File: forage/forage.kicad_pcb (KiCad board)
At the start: 2 copper layers, 308 x 79.4 mm, 68 parts, among them J1 Conn_01x04_MountingPin, Q1 AO3400A, U1 STM32G431RBTx, U2 XC6206P322MR

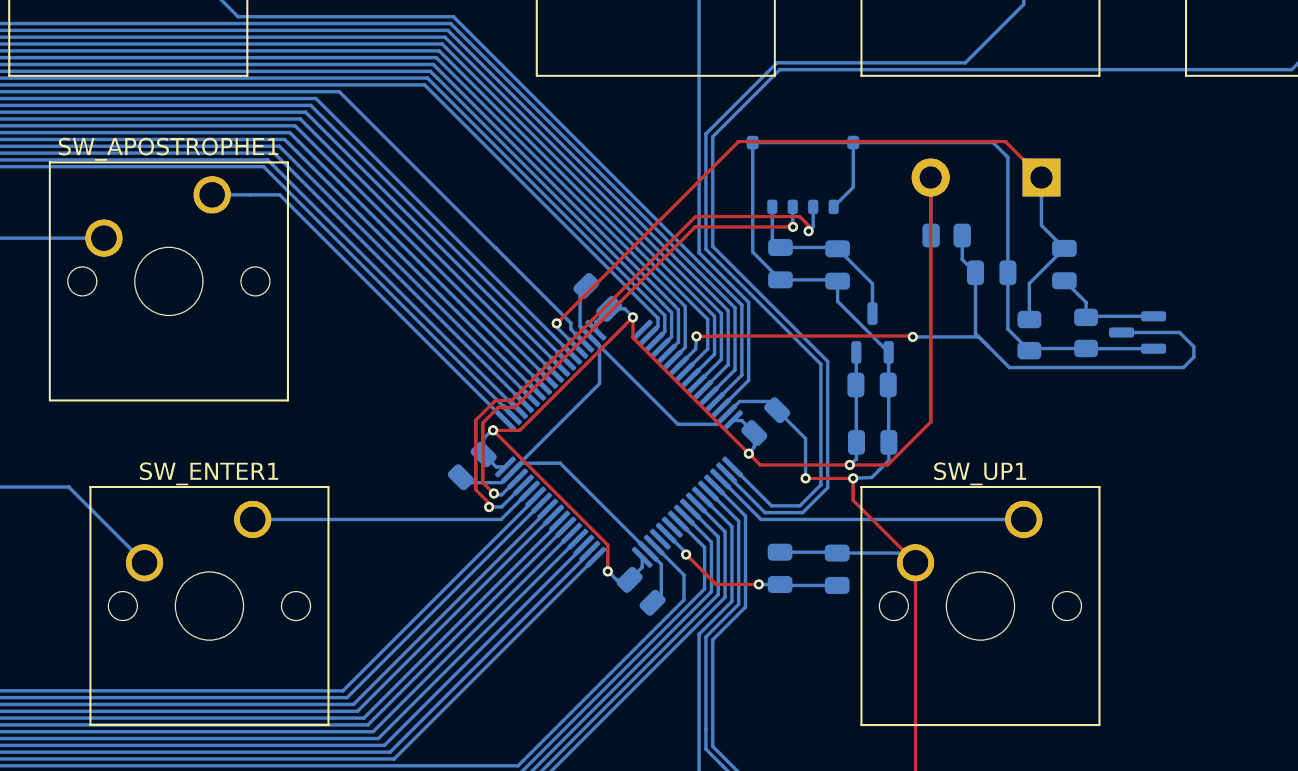
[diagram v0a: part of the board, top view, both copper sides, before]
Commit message: move connector so D+/D- has a direct path
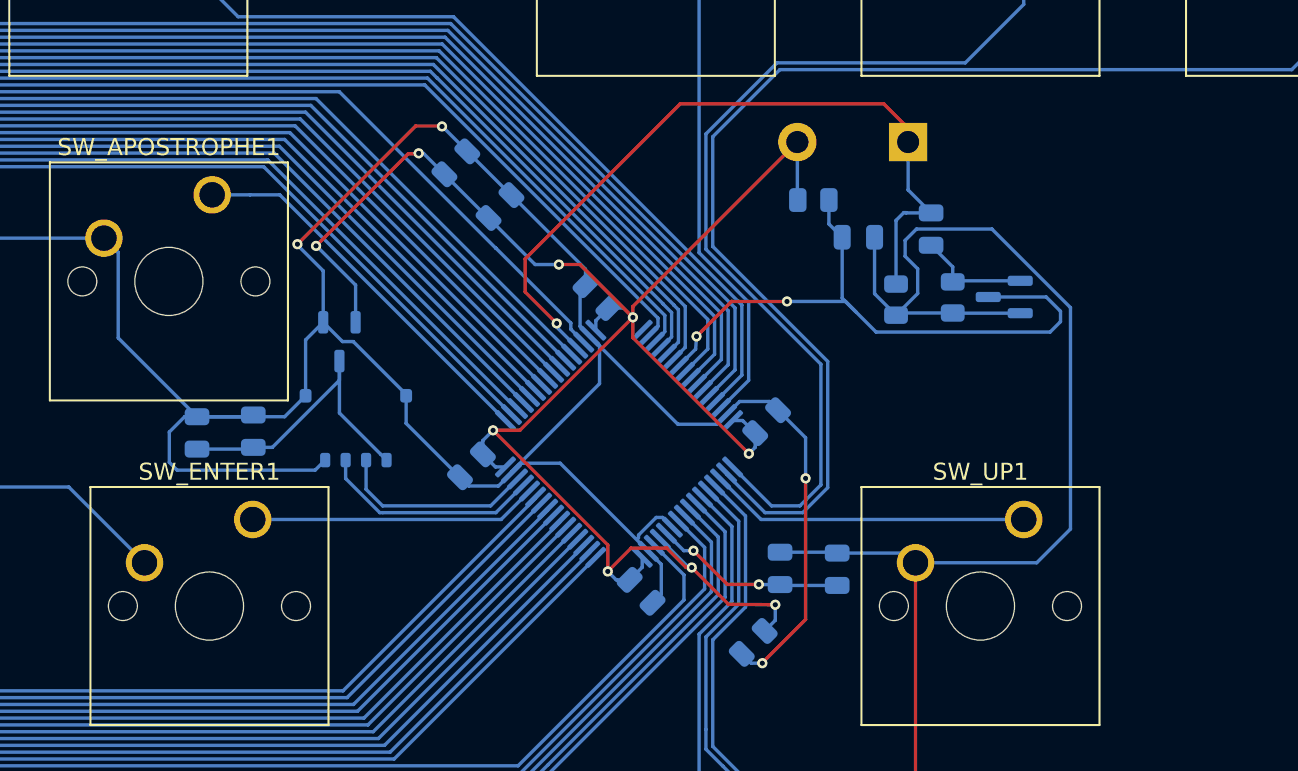
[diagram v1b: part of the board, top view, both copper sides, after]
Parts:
- added C13: 100nF, Capacitor_SMD:C_0805_2012Metric, B.Cu at (316.9, 154.5)
- C12: value 100nF -> 4.7uF
- C6: value 4.7uF -> 100nF
- moved C7 35.7 mm to (284.2, 142.2), turned to 90 degrees
- moved C8 35.7 mm to (287.5, 142.1), turned to 90 degrees
- moved U2 31.3 mm to (292.6, 136.9), turned to -90 degrees
- moved J1 30.2 mm to (293.5, 142.0)
- moved C9 27.7 mm to (299.4, 126.4), turned to 45 degrees
- moved C12 24.1 mm to (302.0, 129.0), turned to 45 degrees
- moved C3 12.4 mm to (310.3, 151.5), turned to -45 degrees
- moved C11 8.10 mm to (323.0, 130.8)
- moved Q1 8.10 mm to (331.6, 134.3)
- moved R1 8.10 mm to (325.2, 134.4)
- moved R2 8.10 mm to (328.6, 134.3)
- moved SW_RESET1 8.10 mm to (326.0, 125.2)
- moved C10 8.10 mm to (327.3, 130.3)
- moved R3 8.10 mm to (320.4, 128.6)
- moved C6 6.34 mm to (317.7, 141.6), turned to 45 degrees
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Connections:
- J1 pad 1: +5V -> GND
- J1 pad 2: D+ -> D-
- J1 pad 3: D- -> D+
- J1 pad 4: GND -> +5V
- U1 pad 27: unconnected-(U1-VSSA-Pad27) -> GND
- U1 pad 29: unconnected-(U1-VDDA-Pad29) -> +3.3V
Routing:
- net GND: track 1305.6 -> 1384.2 mm, vias 2 -> 4
- net +3.3V: track 82.4 -> 110.4 mm, vias 5 -> 9
- net D-: track 34.8 -> 13.0 mm, vias 2 -> 0
- net D+: track 30.8 -> 11.7 mm, vias 2 -> 0
- net +5V: track 10.6 -> 18.1 mm
- net RESET: track 45.0 -> 38.0 mm
- net BOOT: track 45.6 -> 45.1 mm

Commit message: move caps around a little bit to reduce vias
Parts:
- moved C9 14.6 mm to (293.3, 139.6), turned to 180 degrees
- moved C12 11.2 mm to (293.4, 136.1), turned to 180 degrees
- moved J1 6.28 mm to (294.8, 148.1)
- moved U2 5.96 mm to (293.3, 142.8)
- moved C10 3.01 mm to (324.5, 131.5)
- moved C11 3.01 mm to (320.3, 131.9)
- moved Q1 3.01 mm to (328.8, 135.5)
- moved R2 3.01 mm to (325.8, 135.5)
- moved R3 3.01 mm to (317.6, 129.8)
- moved SW_RESET1 3.01 mm to (323.2, 126.4)
- moved R1 3.01 mm to (322.5, 135.6)
- moved C8 2.68 mm to (289.9, 143.5)
- moved C7 2.66 mm to (286.6, 143.5)
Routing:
- net GND: track 1384.2 -> 1332.1 mm, vias 4 -> 2
- net +3.3V: track 110.4 -> 93.4 mm, vias 9 -> 6
- net ENTER: track 16.9 -> 28.5 mm
- net BOOT: track 45.1 -> 36.9 mm
- net RESET: track 38.0 -> 36.7 mm
- net D+: track 11.7 -> 10.3 mm
- net D-: track 13.0 -> 12.0 mm

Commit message: finalize stuff??? who knows
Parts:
- moved C8 0.69 mm to (289.2, 143.5)
- moved C7 0.69 mm to (285.9, 143.5)
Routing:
- net RESET: track 36.7 -> 35.8 mm
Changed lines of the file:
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@@
 	(footprint "Capacitor_SMD:C_0805_2012Metric"
 		(layer "B.Cu")
-		(at 286.5628 143.51 90)
+		(at 285.877 143.5354 90)
 		(descr "Capacitor SMD 0805 (2012 Metric), square (rectangular) end terminal, IPC_7351 nominal, (Body size source: IPC-SM-782 page 76, https://www.pcb-3d.com/wordpress/wp-content/uploads/ipc-sm-782a_amendment_1_and_2.pdf, https://docs.google.com/spreadsheets/d/1BsfQQcO9C6DZCsRaXUlFlo91Tg2WpOkGARC1WS5S8t0/edit?usp=sharing), generated with kicad-footprint-generator")
 		(tags "capacitor")
@@
 	(footprint "Capacitor_SMD:C_0805_2012Metric"
 		(layer "B.Cu")
-		(at 289.8648 143.4592 90)
+		(at 289.179 143.4846 90)
 		(descr "Capacitor SMD 0805 (2012 Metric), square (rectangular) end terminal, IPC_7351 nominal, (Body size source: IPC-SM-782 page 76, https://www.pcb-3d.com/wordpress/wp-content/uploads/ipc-sm-782a_amendment_1_and_2.pdf, https://docs.google.com/spreadsheets/d/1BsfQQcO9C6DZCsRaXUlFlo91Tg2WpOkGARC1WS5S8t0/edit?usp=sharing), generated with kicad-footprint-generator")
 		(tags "capacitor")
@@
 		(tags "SOT TO_SOT_SMD")
 		(property "Reference" "U2"
-			(at 0 2.4 90)
+			(at 0.0199 -2.4892 90)
 			(layer "B.SilkS")
 			(effects
@@
 	)
 	(segment
-		(start 319.3186 131.9492)
-		(end 319.3186 135.5204)
+		(start 319.3186 135.5204)
+		(end 319.3186 131.9492)
 		(width 0.2)
 		(layer "B.Cu")
@@
 	)
 	(segment
-		(start 319.513955 135.715755)
-		(end 320.1162 136.318)
+		(start 332.1304 136.2926)
+		(end 332.1304 136.9022)
 		(width 0.2)
 		(layer "B.Cu")
@@
 	)
 	(segment
-		(start 331.5208 137.5118)
-		(end 332.1304 136.9022)
+		(start 327.8909 135.4544)
+		(end 331.2922 135.4544)
 		(width 0.2)
 		(layer "B.Cu")
@@
 	)
 	(segment
-		(start 313.5376 136.5758)
-		(end 313.4868 136.7028)
+		(start 331.2922 135.4544)
+		(end 332.1304 136.2926)
 		(width 0.2)
 		(layer "B.Cu")
@@
 	)
 	(segment
-		(start 321.31 137.5118)
-		(end 331.5208 137.5118)
+		(start 313.5376 136.5758)
+		(end 313.4868 136.7028)
 		(width 0.2)
 		(layer "B.Cu")
@@
 	)
 	(segment
-		(start 313.4868 137.31854)
-		(end 313.5376 136.5758)
+		(start 321.31 137.5118)
+		(end 319.3186 135.5204)
 		(width 0.2)
 		(layer "B.Cu")
@@
 	)
 	(segment
-		(start 331.2922 135.4544)
-		(end 327.8909 135.4544)
+		(start 331.5208 137.5118)
+		(end 321.31 137.5118)
 		(width 0.2)
 		(layer "B.Cu")
@@
 	)
 	(segment
-		(start 318.5395 129.7648)
-		(end 318.5395 131.1701)
+		(start 313.4868 137.31854)
+		(end 313.5376 136.5758)
 		(width 0.2)
 		(layer "B.Cu")
@@
 	)
 	(segment
-		(start 332.1304 136.2926)
-		(end 331.2922 135.4544)
+		(start 332.1304 136.9022)
+		(end 331.5208 137.5118)
 		(width 0.2)
 		(layer "B.Cu")
@@
 	)
 	(segment
-		(start 320.1162 136.318)
-		(end 321.31 137.5118)
+		(start 318.5395 129.7648)
+		(end 318.5395 131.1701)
 		(width 0.2)
 		(layer "B.Cu")
@@
 		(width 0.2)
 		(layer "B.Cu")
-		(net 7)
-	)
-	(segment
-		(start 332.1304 136.9022)
-		(end 332.1304 136.2926)
-		(width 0.2)
-		(layer "B.Cu")
-		(net 7)
-	)
-	(segment
-		(start 319.3186 135.5204)
-		(end 320.1162 136.318)
-		(width 0.2)
-		(layer "B.Cu")

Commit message: wip: v2
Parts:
- moved J1 1.13 mm to (295.8, 148.7), turned to 90 degrees
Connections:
- U1 pad 49: APOSTROPHE -> SEMICOLON
- U1 pad 50: SEMICOLON -> APOSTROPHE
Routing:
- net PRTSC: track 79.6 -> 62.0 mm
- net RIGHT: track 56.6 -> 45.2 mm
- net DELETE: track 59.7 -> 53.1 mm
- net +5V: track 18.5 -> 13.2 mm
- net D-: track 12.0 -> 7.28 mm
- net D+: track 10.3 -> 7.28 mm
- net COMMA: track 90.2 -> 87.5 mm
- net M: track 110.0 -> 107.3 mm
- net GND: track 1332.1 -> 1334.7 mm, vias 2 -> 3
- net N: track 130.0 -> 127.3 mm
- net DOT: track 70.4 -> 67.8 mm
- net ENTER: track 28.5 -> 25.9 mm
- net B: track 149.8 -> 147.3 mm
- net SLASH: track 50.6 -> 48.2 mm
- net V: track 169.5 -> 167.2 mm
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- added copper zone on B.Cu, net GND

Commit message: fix connector pins.... i think!
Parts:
- moved J1 0.11 mm to (295.7, 148.7)
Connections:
- J1 pad 1: GND -> +5V
- J1 pad 4: +5V -> GND
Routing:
- net +5V: track 13.2 -> 17.1 mm
- net GND: track 1334.7 -> 1333.9 mm
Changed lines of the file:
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@@
 	(footprint "Connector_Molex:Molex_Pico-EZmate_78171-0004_1x04-1MP_P1.20mm_Vertical"
 		(layer "B.Cu")
-		(at 295.795724 148.72 90)
+		(at 295.685724 148.73 90)
 		(descr "Molex Pico-EZmate series connector, 78171-0004 (http://www.molex.com/pdm_docs/sd/781710002_sd.pdf), generated with kicad-footprint-generator")
 		(tags "connector Molex Pico-EZmate side entry")
 		(property "Reference" "J1"
-			(at 5.2908 -1.4224 0)
+			(at -4.64 -0.025724 360)
 			(layer "B.SilkS")
 			(effects
@@
 		)
 		(property "Value" "Conn_01x04_MountingPin"
-			(at 0 -3.72 -90)
+			(at 0 -3.72 270)
 			(layer "B.Fab")
 			(effects
@@
 		)
 		(fp_text user "${REFERENCE}"
-			(at 0 -0.27 -90)
+			(at 0 -0.27 270)
 			(layer "B.Fab")
 			(effects
@@
 			(layers "B.Cu" "B.Paste" "B.Mask")
 			(roundrect_rratio 0.25)
-			(net 1 "GND")
+			(net 4 "+5V")
 			(pinfunction "Pin_1")
 			(pintype "passive")
@@
 			(layers "B.Cu" "B.Paste" "B.Mask")
 			(roundrect_rratio 0.25)
-			(net 4 "+5V")
+			(net 1 "GND")
 			(pinfunction "Pin_4")
 			(pintype "passive")
@@
 	)
 	(segment
-		(start 283.642457 147.363792)
-		(end 281.14625 149.86)
-		(width 0.5)
-		(layer "B.Cu")
-		(net 1)
-	)
-	(segment
-		(start 295.707551 151.67)
-		(end 293.895724 151.67)
-		(width 0.5)
-		(layer "B.Cu")
-		(net 1)
-	)
-	(segment
 		(start 63.420625 167.560625)
 		(end 62.07125 168.91)
@@
 	)
 	(segment
+		(start 297.560724 146.93)
+		(end 300 146.93)
+		(width 0.5)
+		(layer "B.Cu")
+		(net 1)
+	)
+	(segment
 		(start 170.808963 145.77)
 		(end 177.171036 145.77)
@@
 	)
 	(segment
+		(start 299.90735 145.79735)
+		(end 300.345 146.235)
+		(width 0.5)
+		(layer "B.Cu")
+		(net 1)
+	)
+	(segment
 		(start 311.739376 147.391142)
 		(end 312.119948 147.771714)
@@
 	)
 	(segment
+		(start 300.345 146.235)
+		(end 300.52 146.41)
+		(width 0.5)
+		(layer "B.Cu")
+		(net 1)
+	)
+	(segment
 		(start 171.493792 109.263792)
 		(end 173.99 111.76)
@@
 	)
 	(segment
-		(start 297.095724 151.095)
-		(end 297.670724 150.52)
+		(start 64.61125 150.01875)
+		(end 64.4525 149.86)
 		(width 0.5)
 		(layer "B.Cu")
@@
 	)
 	(segment
-		(start 64.61125 150.01875)
-		(end 64.4525 149.86)
+		(start 293.775724 145.77)
+		(end 293.785724 145.78)
 		(width 0.5)
 		(layer "B.Cu")
@@
 	)
 	(segment
+		(start 300 146.93)
+		(end 300.52 146.41)
+		(width 0.5)
+		(layer "B.Cu")
+		(net 1)
+	)
+	(segment
 		(start 262.211207 147.363792)
 		(end 259.715 149.86)
@@
 	)
 	(segment
-		(start 293.895724 151.67)
-		(end 293.895724 145.77)
-		(width 0.5)
-		(layer "B.Cu")
-		(net 1)
-	)
-	(segment
 		(start 332.733963 107.67)
 		(end 339.096036 107.67)
@@
 	)
 	(segment
+		(start 285.21625 145.79)
+		(end 286.3 145.79)
+		(width 0.5)
+		(layer "B.Cu")
+		(net 1)
+	)
+	(segment
 		(start 257.218792 147.363792)
 		(end 259.715 149.86)
@@
 	)
 	(segment
+		(start 286.32 145.77)
+		(end 293.775724 145.77)
+		(width 0.5)
+		(layer "B.Cu")
+		(net 1)
+	)
+	(segment
 		(start 300.533002 145.354804)
 		(end 301.374015 145.354804)
@@
 	)
 	(segment
+		(start 293.785724 151.68)
+		(end 293.785724 145.78)
+		(width 0.5)
+		(layer "B.Cu")
+		(net 1)
+	)
+	(segment
 		(start 310.08481 148.225097)
 		(end 310.08481 148.565004)
@@
 	)
 	(segment
-		(start 299.90735 145.79735)
-		(end 300.52 146.41)
-		(width 0.5)
-		(layer "B.Cu")
-		(net 1)
-	)
-	(segment
-		(start 287.490213 145.77)
-		(end 293.895724 145.77)
-		(width 0.5)
-		(layer "B.Cu")
-		(net 1)
-	)
-	(segment
 		(start 247.693792 109.263792)
 		(end 250.19 111.76)
@@
 	)
 	(segment
+		(start 281.14625 149.86)
+		(end 285.21625 145.79)
+		(width 0.5)
+		(layer "B.Cu")
+		(net 1)
+	)
+	(segment
 		(start 186.011207 147.363792)
 		(end 183.515 149.86)
@@
 		(net 1)
 	)
+	(segment
+		(start 286.3 145.79)
+		(end 286.32 145.77)
+		(width 0.5)
+		(layer "B.Cu")
+		(net 1)
+	)
 	(arc
 		(start 273.887542 109.263792)
@@
 	)
 	(arc
-		(start 287.490213 145.77)
-		(mid 285.407822 146.184213)
-		(end 283.642457 147.363792)
-		(width 0.5)
-		(layer "B.Cu")
-		(net 1)
-	)
-	(arc
 		(start 314.991467 141.470728)
 		(mid 314.647584 141.700503)
@@
 	)
 	(arc
-		(start 297.095724 151.095)
-		(mid 296.458824 151.520562)
-		(end 295.707551 151.67)
-		(width 0.5)
-		(layer "B.Cu")
-		(net 1)
-	)
-	(arc
 		(start 280.948292 149.808292)
 		(mid 281.005566 149.846561)
@@
 	)
 	(segment
-		(start 294.930297 144.179573)
-		(end 297.670724 146.92)
+		(start 285.9278 144.4346)
+		(end 285.877 144.4854)
 		(width 0.3)
 		(layer "B.Cu")
@@
 	)
 	(segment
-		(start 293.683738 143.9418)
+		(start 293.2405 143.9418)
 		(end 293.3192 143.9418)
 		(width 0.3)
@@
 	)
 	(segment
-		(start 285.9278 144.4346)
-		(end 285.877 144.4854)
+		(start 293.9618 143.9418)
+		(end 295.07 145.05)
 		(width 0.3)
 		(layer "B.Cu")
@@
 	)
 	(segment
-		(start 293.2405 143.9418)
-		(end 293.3192 143.9418)
+		(start 292.320537 144.4346)
+		(end 289.179 144.4346)
 		(width 0.3)
 		(layer "B.Cu")
@@
 	)
 	(segment
-		(start 292.320537 144.4346)
-		(end 289.179 144.4346)
+		(start 296.19 150.53)
+		(end 297.560724 150.53)
 		(width 0.3)
 		(layer "B.Cu")
@@
 	)
 	(segment
-		(start 294.356262 143.9418)
-		(end 293.683738 143.9418)
+		(start 295.07 149.41)
+		(end 296.19 150.53)
 		(width 0.3)
 		(layer "B.Cu")
@@
 		(net 4)
 	)
+	(segment
+		(start 293.3192 143.9418)
+		(end 293.9618 143.9418)
+		(width 0.3)
+		(layer "B.Cu")
+		(net 4)
+	)
+	(segment
+		(start 295.07 145.05)
+		(end 295.07 149.41)
+		(width 0.3)
+		(layer "B.Cu")
+		(net 4)
+	)
 	(arc
 		(start 292.915399 144.188199)
@@
 		(net 4)
 	)
-	(arc
-		(start 294.930297 144.179573)
-		(mid 294.666927 144.003595)
-		(end 294.356262 143.9418)
-		(width 0.3)
-		(layer "B.Cu")
-		(net 4)
-	)
 	(segment
 		(start 324.5358 132.8579)
@@
 	)
 	(segment
+		(start 297.670724 148.12)
+		(end 297.660724 148.11)
+		(width 0.3)
+		(layer "B.Cu")
+		(net 8)
+	)
+	(segment
 		(start 298.874 147.61)
 		(end 298.99 147.61)
@@
 		(width 0.3)
 		(layer "B.Cu")
+		(net 9)
+	)
+	(segment
+		(start 297.670724 149.32)
+		(end 297.660724 149.31)
+		(width 0.3)
+		(layer "B.Cu")
